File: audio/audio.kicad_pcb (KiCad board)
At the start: 2 copper layers, 52 x 26 mm, 71 parts, among them P1 CONN_02X01, P2 CONN_01X04, P3 CONN_02X01, U1 PCM2912A, U2 MIC, U3 FB, U4 FB, U5 NAU8223, U6 FB, U7 FB, X1 6MHz

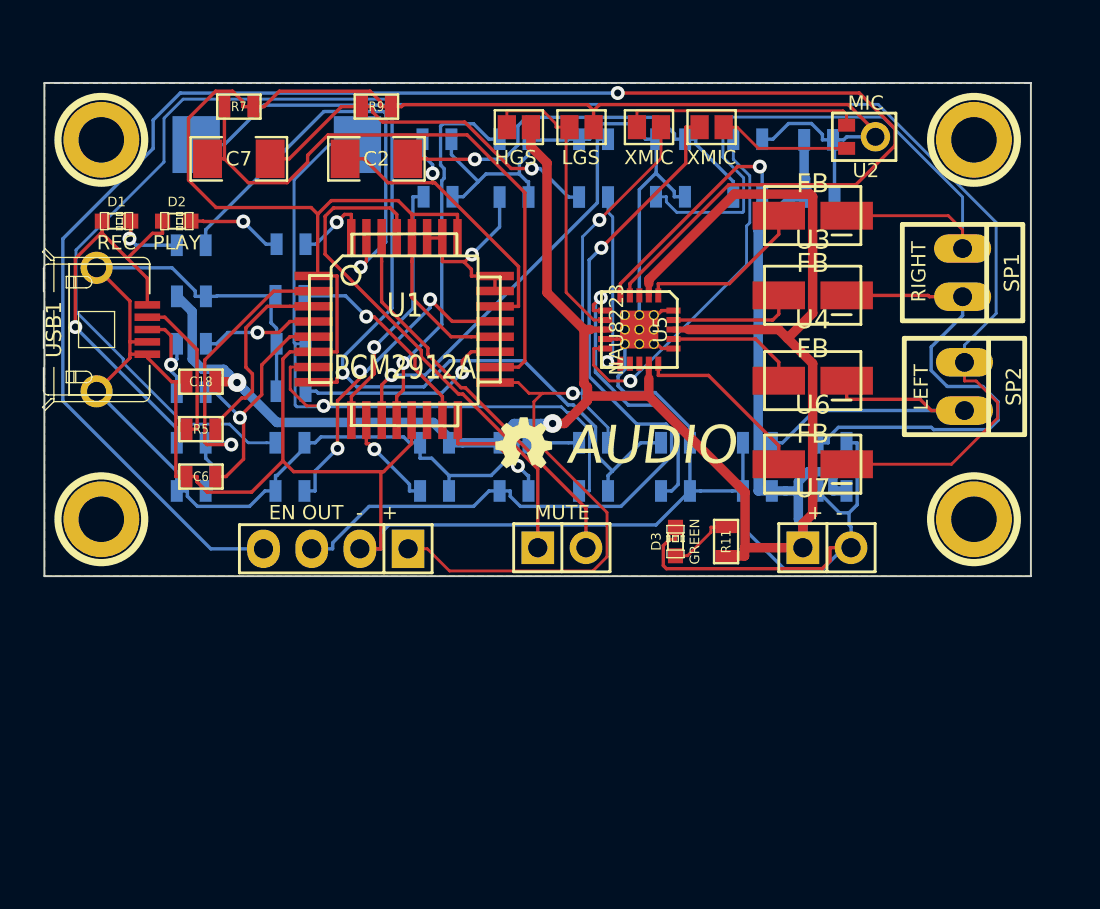
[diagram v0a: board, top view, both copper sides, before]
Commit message: finished schematic. need to route board and send BOM
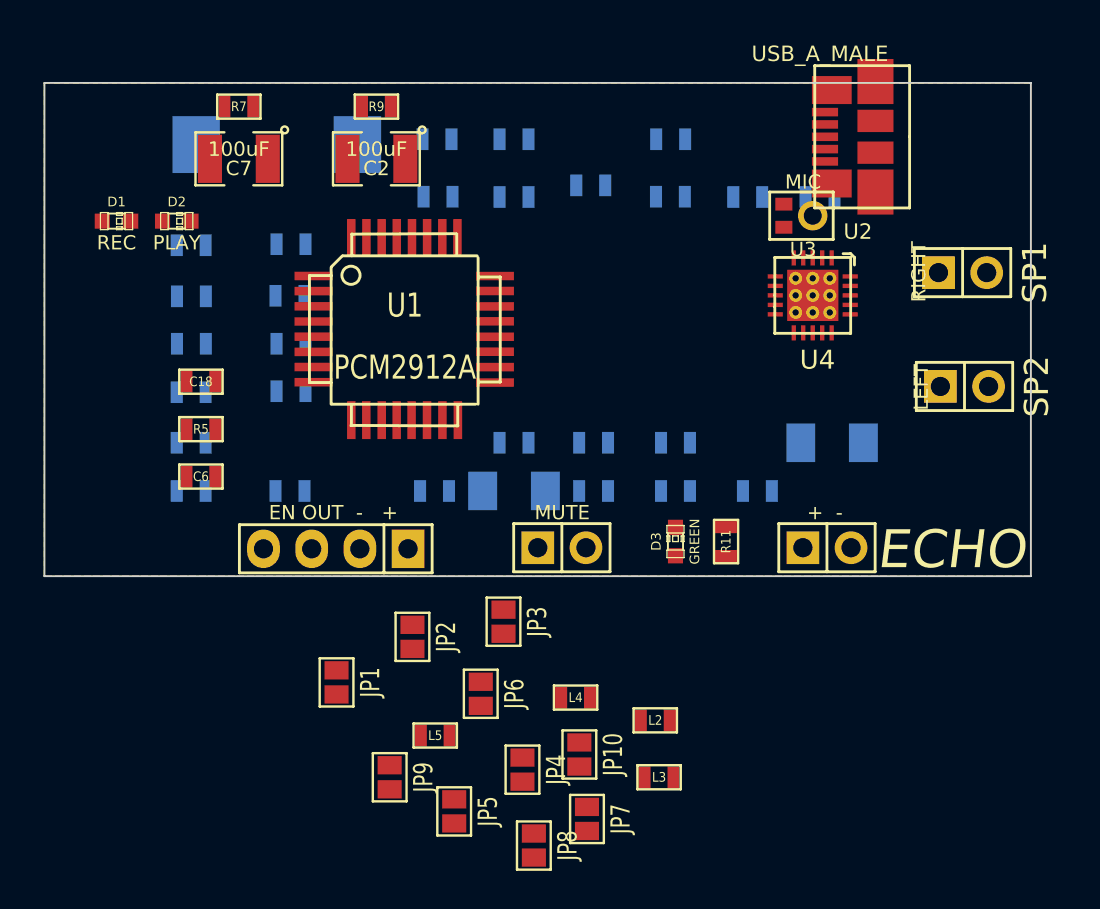
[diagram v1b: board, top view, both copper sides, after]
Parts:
- removed C26, C32: 10uF, SMD_Packages:SMD-0603
- removed C27, C29: 0.47uF, SMD_Packages:SMD-0603
- removed C28, C30: 1nF, SMD_Packages:SMD-0603
- removed C31: 0.1uF, SMD_Packages:SMD-0603
- removed G***: LOGO, MIC:logo
- removed G***: LOGO, MIC:OSLOGO
- removed PIN1, PIN2, PIN3, PIN4: PIN1, Connect:1pin
- removed U5: NAU8223, MIC:QFN20
- removed U6, U7: FB, MIC:FB-28F0121
- removed USB1: AB2_USB, AB2USB:AB2_USB_MICRO_SMD
- added JP10: JUMPER, Connect:GS2, F.Cu at (153.1, 126.5)
- added JP5: JUMPER, Connect:GS2, F.Cu at (146.4, 129.5)
- added JP6: JUMPER, Connect:GS2, F.Cu at (147.8, 123.3)
- added JP7: JUMPER, Connect:GS2, F.Cu at (153.4, 129.9)
- added JP8: JUMPER, Connect:GS2, F.Cu at (150.7, 131.3)
- added JP9: JUMPER, Connect:GS2, F.Cu at (143.1, 127.7)
- added L2: FERRITE, SMD_Packages:SMD-0603, F.Cu at (157.1, 124.7)
- added L3: FERRITE, SMD_Packages:SMD-0603, F.Cu at (157.2, 127.7)
- added L4: FERRITE, SMD_Packages:SMD-0603, F.Cu at (152.8, 123.5)
- added L5: FERRITE, SMD_Packages:SMD-0603, F.Cu at (145.4, 125.5)
- C10: value 2.2uF -> 10uF; footprint SMD_Packages:SMD-0603 -> SMD_Packages:SMD-1206
- C12, C9: value 0.1uF -> .1uF
- C13: value 3u3 -> 3.3uF
- C16, C8: value 22pF -> 33pF
- C17: value 0.1uF -> 1uF
- C18: value 10uF -> 1uF
- C19: value 1nF -> 1uF
- C2, C7: footprint SMD_Packages:SMD-1206 -> SMD_Packages:SMD-1210
- C20: value 0.47uF -> 1uF
- C21: value 1nF -> 10uF; footprint SMD_Packages:SMD-0603 -> SMD_Packages:SMD-1206
- C22: value 0.47uF -> 1nF
- C23: value 10uF -> 1nF
- C24, C25: value 0.1uF -> 1nF
- D1: value RED -> GREEN
- JP3: value HGS -> JUMPER
- JP4: value LGS -> JUMPER
- R1, R2: value 1K5 -> 1k
- R11: value 510R -> 1k
- SP1: value RIGHT -> SPEAKER; footprint Connect:PINHEAD1-2 -> Pin_Headers:Pin_Header_Straight_2x01
- SP2: value LEFT -> SPEAKER; footprint Connect:PINHEAD1-2 -> Pin_Headers:Pin_Header_Straight_2x01
- U2: value MIC -> USB_A_MALE; footprint MIC:MIC -> apro-lib:MICRO_USB
- U3: value FB -> MIC; footprint MIC:FB-28F0121 -> apro-lib:MIC
- U4: value FB -> TPA2017D2; footprint MIC:FB-28F0121 -> apro-lib:TPA2017D2
- X1: footprint MIC:FOX6MHZ -> apro-lib:FOX6MHZ
- moved JP4 34.0 mm to (150.1, 127.3), turned to 0 degrees
- moved JP1 33.6 mm to (140.2, 122.7), turned to 0 degrees
- moved JP2 31.2 mm to (144.2, 120.3), turned to 0 degrees
- moved JP3 26.1 mm to (149.1, 119.5), turned to 0 degrees
- moved C13 2.44 mm to (153.7, 96.5)
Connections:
- C1 pad 1: XGND -> Net-(C1-Pad1)
- C1 pad 2: Net-(C1-Pad2) -> XGND
- C10 pad 1: Net-(C10-Pad1) -> XOUT
- C10 pad 2: XOUT -> Net-(C10-Pad2)
- C12 pad 1: Net-(C12-Pad1) -> XGND
- C12 pad 2: XGND -> Net-(C12-Pad2)
- C13 pad 1: Net-(C13-Pad1) -> XGND
- C13 pad 2: XGND -> Net-(C13-Pad2)
- C14 pad 1: Net-(C14-Pad1) -> XGND
- C14 pad 2: XGND -> Net-(C14-Pad2)
- C15 pad 1: Net-(C15-Pad1) -> XGND
- C15 pad 2: XGND -> Net-(C15-Pad2)
- C17 pad 1: +5VA -> Net-(C17-Pad1)
- C18 pad 1: +5VA -> Net-(C18-Pad1)
- C18 pad 2: XGND -> L_IN
- C2 pad 1: R_IN -> Net-(C2-Pad1)
- C21 pad 1: Net-(C21-Pad1) -> XGND
- C21 pad 2: XGND -> +5VA
- C22 pad 1: Net-(C22-Pad1) -> XGND
- C22 pad 2: XGND -> Net-(C22-Pad2)
- C23 pad 1: +5VA -> XGND
- C23 pad 2: XGND -> Net-(C23-Pad2)
- C24 pad 1: +5VA -> XGND
- C24 pad 2: XGND -> Net-(C24-Pad2)
- C25 pad 1: +5VA -> XGND
- C25 pad 2: XGND -> Net-(C25-Pad2)
- C7 pad 1: L_IN -> Net-(C7-Pad1)
- C9 pad 1: XPWR -> XGND
- C9 pad 2: XGND -> XPWR
- JP1 pad 1: XPWR -> R_IN
- JP1 pad 2: Net-(JP1-Pad2) -> Net-(C2-Pad1)
- JP2 pad 1: XOUT -> Net-(C2-Pad2)
- JP2 pad 2: Net-(JP2-Pad2) -> R_IN
- JP3 pad 1: +5VA -> L_IN
- JP3 pad 2: Net-(JP3-Pad2) -> Net-(C7-Pad2)
- JP4 pad 1: XGND -> Net-(C7-Pad1)
- JP4 pad 2: Net-(JP3-Pad2) -> L_IN
- R3 pad 2: R_IN -> Net-(C2-Pad1)
- R9 pad 1: L_IN -> Net-(C7-Pad1)
- SP1 pad 1: Net-(C19-Pad1) -> Net-(C22-Pad2)
- SP1 pad 2: Net-(C21-Pad1) -> Net-(C23-Pad2)
- SP2 pad 1: Net-(C30-Pad1) -> Net-(C24-Pad2)
- SP2 pad 2: Net-(C28-Pad1) -> Net-(C25-Pad2)
- U1 pad 10: Net-(C14-Pad1) -> Net-(C14-Pad2)
- U1 pad 11: Net-(C13-Pad1) -> Net-(C13-Pad2)
- U1 pad 12: Net-(C12-Pad1) -> Net-(C12-Pad2)
- U1 pad 16: Net-(C10-Pad1) -> Net-(C10-Pad2)
- U1 pad 23: Net-(C1-Pad2) -> Net-(C1-Pad1)
- U1 pad 24: Net-(C1-Pad2) -> Net-(C1-Pad1)
- U1 pad 26: Net-(C1-Pad2) -> Net-(C1-Pad1)
- U1 pad 27: Net-(C1-Pad2) -> Net-(C1-Pad1)
- U1 pad 9: Net-(C15-Pad1) -> Net-(C15-Pad2)
- U2 pad 1: Net-(JP2-Pad2) -> Net-(D1-Pad1)
- U2 pad 2: XGND -> Net-(R5-Pad2)
- U2 pad 3: Net-(JP1-Pad2) -> Net-(R6-Pad2)
- U3 pad 1: Net-(C19-Pad1) -> Net-(JP6-Pad2)
- U3 pad 2: Net-(U3-Pad2) -> XGND
- U4 pad 1: Net-(C21-Pad1) -> Net-(C18-Pad1)
- U4 pad 2: Net-(U4-Pad2) -> Net-(C17-Pad1)
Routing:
- net XGND: track 289.6 -> 0.00 mm
- net +5VA: track 131.7 -> 0.00 mm, vias 2 -> 0
- net Net-(C30-Pad1): track 93.7 -> 0.00 mm
- net EN: track 89.6 -> 0.00 mm, vias 1 -> 0
- net Net-(C16-Pad1): track 50.7 -> 0.00 mm, vias 1 -> 0
- net XPWR: track 45.4 -> 0.00 mm, vias 2 -> 0
- net XOUT: track 44.9 -> 0.00 mm, vias 1 -> 0
- net Net-(C8-Pad1): track 41.0 -> 0.00 mm, vias 1 -> 0
- net Net-(C19-Pad1): track 34.8 -> 0.00 mm
- net Net-(C7-Pad2): track 33.1 -> 0.00 mm
- net Net-(P1-Pad1): track 27.6 -> 0.00 mm
- net Net-(C21-Pad1): track 26.2 -> 0.00 mm
- net Net-(R1-Pad1): track 23.2 -> 0.00 mm, vias 1 -> 0
- net Net-(D1-Pad1): track 22.4 -> 0.00 mm, vias 1 -> 0
- net R_IN: track 21.2 -> 0.00 mm, vias 1 -> 0
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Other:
- board text added: "ECHO"
- board text removed: "AUDIO"
- board text removed: "HGS"
- board text removed: "LGS"
- board text removed: "XMIC"

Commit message: finished board layout. Ready for review
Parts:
- C1, C10, C11, C12, C13, C14, C15, C16, C17, C19, C20, C21, C22, C23, C24, C25, C3, C4, C5, C8, C9, L1, R1, R10, R2, R3, R4, R6, R8, X1: moved to F.Cu
- moved U2 42.8 mm to (127.0, 104.1), turned to 0 degrees
- moved C18 33.4 mm to (166.4, 107.1), turned to 0 degrees
- moved P1 31.9 mm to (126.2, 96.9), turned to 180 degrees
- moved JP4 31.0 mm to (157.8, 97.3), turned to 180 degrees
- moved L5 29.3 mm to (159.7, 99.9), turned to 90 degrees
- moved C24 29.1 mm to (161.2, 97.3), turned to 270 degrees
- moved L3 28.4 mm to (162.8, 99.9), turned to 90 degrees
- moved JP1 26.3 mm to (144.1, 96.7), turned to 180 degrees
- moved L2 25.9 mm to (164.4, 99.9), turned to 90 degrees
- moved JP8 25.8 mm to (166.4, 110.9), turned to 270 degrees
- moved C16 25.5 mm to (132.7, 109.7), turned to 180 degrees
- moved L4 25.1 mm to (161.2, 99.9), turned to 90 degrees
- moved JP7 24.7 mm to (166.4, 108.9), turned to 270 degrees
- moved JP2 23.7 mm to (146.1, 96.7), turned to 180 degrees
- moved JP3 23.2 mm to (155.8, 97.3)
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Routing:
- net XGND: track 0.00 -> 205.0 mm
- net +5VA: track 0.00 -> 56.2 mm, vias 0 -> 3
- net Net-(C8-Pad1): track 0.00 -> 28.9 mm
- net Net-(C25-Pad2): track 0.00 -> 27.7 mm, vias 0 -> 1
- net R_IN: track 0.00 -> 21.4 mm
- net L_IN: track 0.00 -> 21.3 mm
- net Net-(P1-Pad2): track 0.00 -> 16.8 mm
- net Net-(P1-Pad1): track 0.00 -> 16.8 mm
- net XOUT: track 0.00 -> 16.1 mm
- net Net-(C7-Pad2): track 0.00 -> 16.0 mm, vias 0 -> 2
- net Net-(C24-Pad2): track 0.00 -> 15.6 mm
- net Net-(JP7-Pad2): track 0.00 -> 15.0 mm, vias 0 -> 2
- net Net-(C7-Pad1): track 0.00 -> 14.0 mm
- net XPWR: track 0.00 -> 13.7 mm
- net Net-(C23-Pad2): track 0.00 -> 11.2 mm
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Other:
- board size 52 x 26 mm -> 47 x 21.8 mm
- net class Default: via_dia 0.7366 -> 0.6858; via_drill 0.381 -> 0.3302
- net class power: trace_width 0.5 -> 0.4572
- rule via_min_drill: 0.381 -> 0.3302
- rule via_min_size: 0.7366 -> 0.6858
- board text added: "EN"
- board text added: "XGND"
- board text added: "XOUT"
- board text added: "XPWR"
- board text removed: "+ -"
- board text removed: "EN OUT - +"
- board text removed: "MUTE"
- board text removed: "PLAY"
- board text removed: "REC"
